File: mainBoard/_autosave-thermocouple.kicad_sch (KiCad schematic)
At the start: 18 parts, among them J10 4DB-P108-02, U5 OPA333AIDCKT, U7 DS18B20+

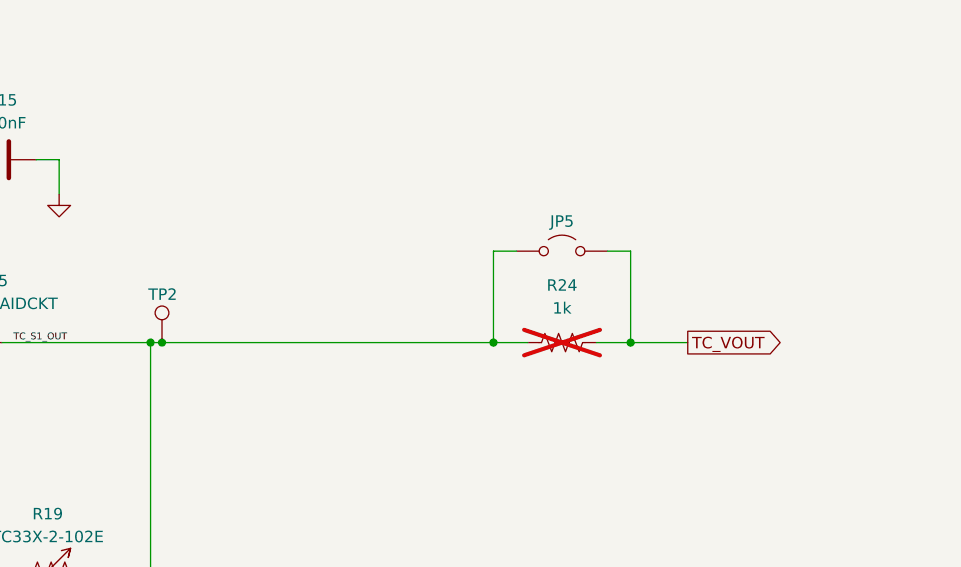
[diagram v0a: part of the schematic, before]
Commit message: Add net colors and tweak MCU
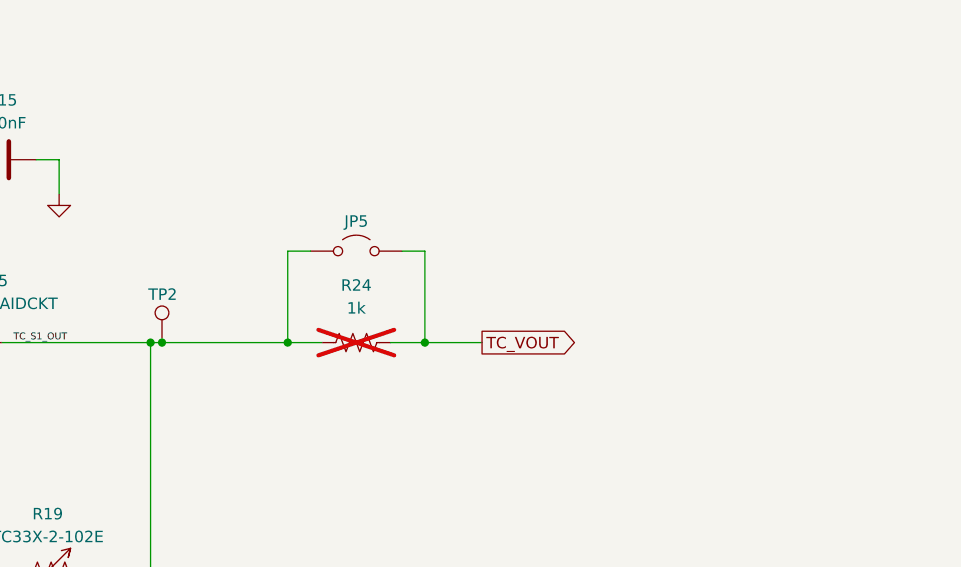
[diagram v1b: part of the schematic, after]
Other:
- moved on the sheet: JP5, R24
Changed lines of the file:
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@@
 	)
 	(junction
-		(at 280.67 115.57)
+		(at 257.81 115.57)
 		(diameter 0)
 		(color 0 0 0 0)
@@
 	)
 	(junction
-		(at 295.91 115.57)
+		(at 273.05 115.57)
 		(diameter 0)
 		(color 0 0 0 0)
@@
 	(wire
 		(pts
-			(xy 283.21 105.41) (xy 280.67 105.41)
+			(xy 260.35 105.41) (xy 257.81 105.41)
 		)
 		(stroke
@@
 	(wire
 		(pts
-			(xy 243.84 115.57) (xy 280.67 115.57)
+			(xy 243.84 115.57) (xy 257.81 115.57)
 		)
 		(stroke
@@
 	(wire
 		(pts
-			(xy 295.91 105.41) (xy 295.91 115.57)
-		)
-		(stroke
-			(width 0)
-			(type default)
-		)
-	)
-	(wire
-		(pts
-			(xy 292.1 115.57) (xy 295.91 115.57)
+			(xy 273.05 105.41) (xy 273.05 115.57)
+		)
+		(stroke
+			(width 0)
+			(type default)
+		)
+	)
+	(wire
+		(pts
+			(xy 269.24 115.57) (xy 273.05 115.57)
 		)
 		(stroke
@@
 	(wire
 		(pts
-			(xy 293.37 105.41) (xy 295.91 105.41)
+			(xy 270.51 105.41) (xy 273.05 105.41)
 		)
 		(stroke
@@
 	(wire
 		(pts
-			(xy 280.67 105.41) (xy 280.67 115.57)
+			(xy 257.81 105.41) (xy 257.81 115.57)
 		)
 		(stroke
@@
 	(wire
 		(pts
-			(xy 280.67 115.57) (xy 284.48 115.57)
+			(xy 257.81 115.57) (xy 261.62 115.57)
 		)
 		(stroke
@@
 	(wire
 		(pts
-			(xy 295.91 115.57) (xy 302.26 115.57)
+			(xy 273.05 115.57) (xy 279.4 115.57)
 		)
 		(stroke
@@
 	(global_label "TC_VOUT"
 		(shape output)
-		(at 302.26 115.57 0)
+		(at 279.4 115.57 0)
 		(fields_autoplaced yes)
 		(effects
@@
 		)
 		(property "Intersheetrefs" "${INTERSHEET_REFS}"
-			(at 313.1676 115.57 0)
+			(at 290.3076 115.57 0)
 			(effects
 				(font
@@
 	(symbol
 		(lib_id "Device:R_US")
-		(at 288.29 115.57 90)
+		(at 265.43 115.57 90)
 		(unit 1)
 		(exclude_from_sim no)
@@
 		(fields_autoplaced yes)
 		(property "Reference" "R24"
-			(at 288.29 109.22 90)
+			(at 265.43 109.22 90)
 			(effects
 				(font
@@
 		)
 		(property "Value" "1k"
-			(at 288.29 111.76 90)
+			(at 265.43 111.76 90)
 			(effects
 				(font
@@
 		)
 		(property "Footprint" "Resistor_SMD:R_0603_1608Metric_Pad0.98x0.95mm_HandSolder"
-			(at 288.544 114.554 90)
+			(at 265.684 114.554 90)
 			(effects
 				(font
@@
 		)
 		(property "Datasheet" "~"
-			(at 288.29 115.57 0)
+			(at 265.43 115.57 0)
 			(effects
 				(font
@@
 		)
 		(property "Description" "Resistor, US symbol"
-			(at 288.29 115.57 0)
+			(at 265.43 115.57 0)
 			(effects
 				(font
@@
 	(symbol
 		(lib_id "Jumper:Jumper_2_Open")
-		(at 288.29 105.41 0)
+		(at 265.43 105.41 0)
 		(unit 1)
 		(exclude_from_sim no)
@@
 		(dnp no)
 		(property "Reference" "JP5"
-			(at 288.29 102.108 0)
+			(at 265.43 102.108 0)
 			(effects
 				(font
@@
 		)
 		(property "Value" "Jumper_2_Open"
-			(at 288.29 101.6 0)
+			(at 265.43 101.6 0)
 			(effects
 				(font
@@
 		)
 		(property "Footprint" "Jumper:SolderJumper-2_P1.3mm_Open_TrianglePad1.0x1.5mm"
-			(at 288.29 105.41 0)
+			(at 265.43 105.41 0)
 			(effects
 				(font
@@
 		)
 		(property "Datasheet" "~"
-			(at 288.29 105.41 0)
+			(at 265.43 105.41 0)
 			(effects
 				(font
@@
 		)
 		(property "Description" "Jumper, 2-pole, open"
-			(at 288.29 105.41 0)
-			(effects
-				(font
+			(at 265.43 105.41 0)
+			(effects
+				(font
